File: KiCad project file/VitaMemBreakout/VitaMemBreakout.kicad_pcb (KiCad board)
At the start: 2 copper layers, 24.5 x 43 mm, 2 parts

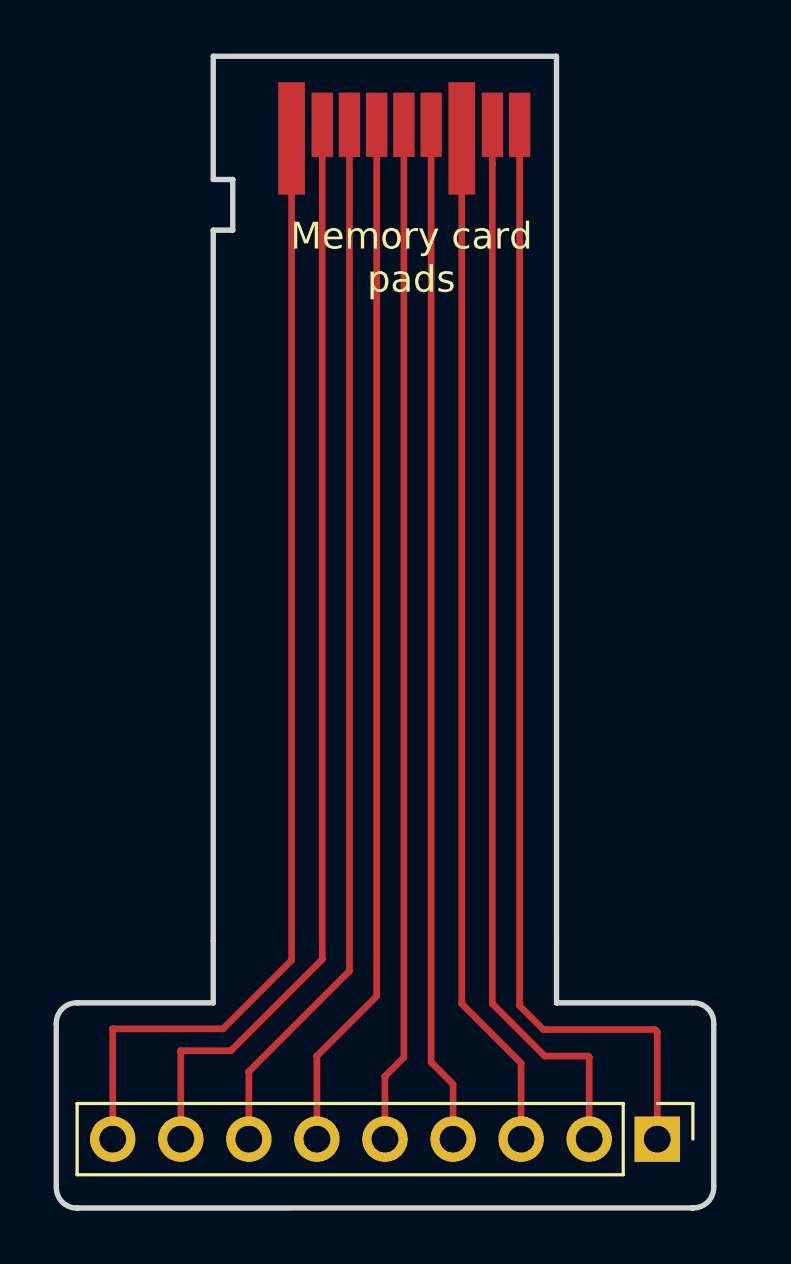
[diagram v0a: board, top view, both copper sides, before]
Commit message: Updated Pins
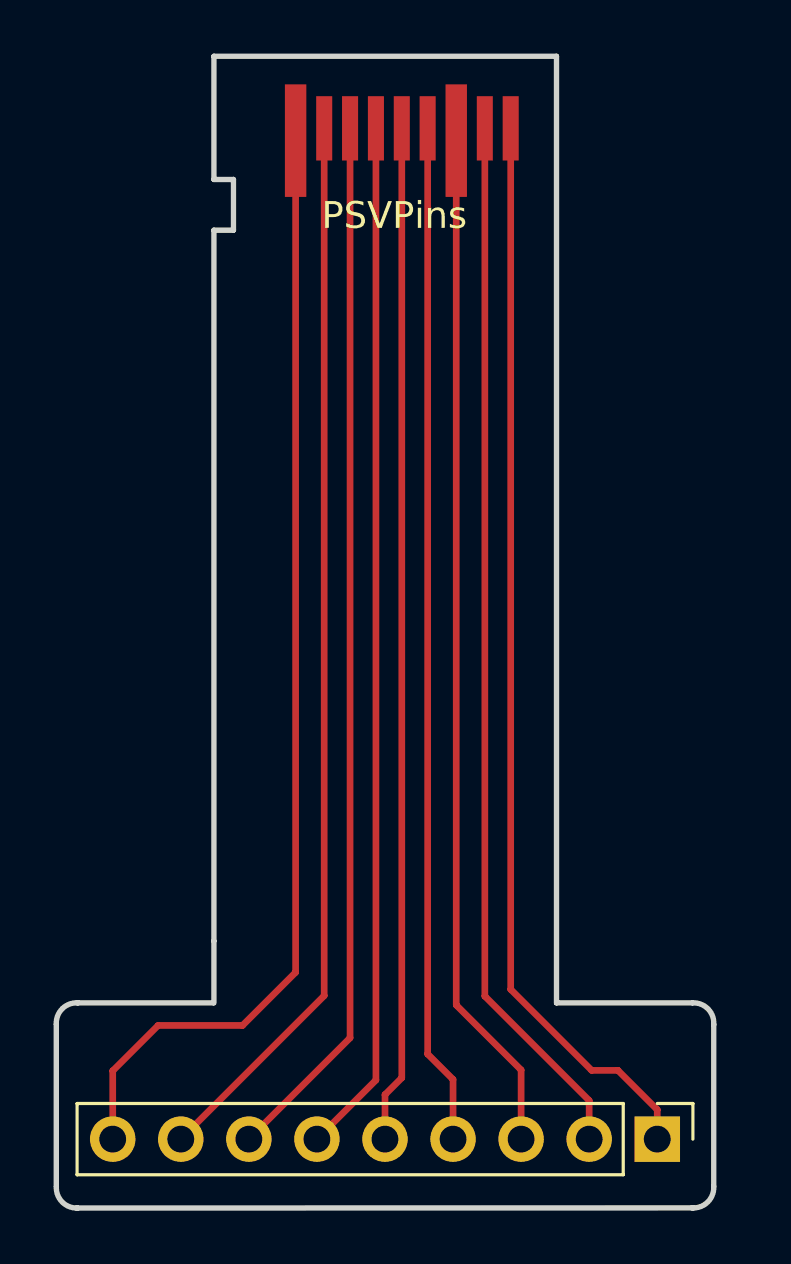
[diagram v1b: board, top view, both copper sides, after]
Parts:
- removed the ? at (30.3, 17.3)
- added PSVPins: , PSVita:PSVitaEdgeConnector, F.Cu at (30.5, 17.3)
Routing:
- net (no net): track 359.2 -> 354.0 mm
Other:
- board text removed: "Memory card pads"

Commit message: Hopefully perfect
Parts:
- removed PSVPins: , PSVita:PSVitaEdgeConnector
- added ?: , PSVita:PSVitaEdgeConnector, F.Cu at (30.4, 17.3)
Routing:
- net (no net): track 354.0 -> 352.3 mm
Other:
- outline, holes or cut-outs redrawn
- board text added: "By motoharu & TakuyaKou"

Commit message: V.Final
Production ready!
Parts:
- moved ? 0.40 mm to (39.3, 55.2)
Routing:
- net (no net): track 352.3 -> 353.2 mm
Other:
- board size 24.5 x 43 mm -> 25.3 x 43 mm
- board text added: "v 0.999"
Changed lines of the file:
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@@
   (general
     (thickness 1.6)
-    (drawings 21)
+    (drawings 22)
     (tracks 18)
     (zones 0)
@@
     (34 B.Paste user)
     (35 F.Paste user)
-    (36 B.SilkS user hide)
+    (36 B.SilkS user)
     (37 F.SilkS user)
     (38 B.Mask user)
@@
   )
   (module Connector_PinHeader_2.54mm:PinHeader_1x09_P2.54mm_Vertical (layer F.Cu)
-    (at 38.89502 55.118 270)
+    (at 39.2938 55.1688 270)
     (descr "Through hole straight pin header, 1x09, 2.54mm pitch, single row")
     (tags "Through hole pin header THT 1x09 2.54mm single row")
@@
     )
   )
-  (gr_text "By motoharu & TakuyaKou" (at 32.258 36.576 90) (layer B.SilkS)
+  (gr_text "v 0.999" (at 20.7645 51.6128) (layer B.SilkS)
+    (effects (font (size 1 1) (thickness 0.25)) (justify mirror))
+  )
+  (gr_text "By motoharu & TakuyaKou" (at 32.7025 31.5976 90) (layer B.SilkS)
     (effects (font (size 1.5 1.5) (thickness 0.3)) (justify mirror))
   )
   (gr_line (start 35.13582 47.72914) (end 35.13582 14.70914) (layer Edge.Cuts) (width 0.2))
   (gr_arc (start 17.228796 56.930987) (end 16.471876 56.885267) (angle -96.1) (layer Edge.Cuts) (width 0.2))
-  (gr_arc (start 40.245756 56.926504) (end 40.200036 57.683424) (angle -96.1) (layer Edge.Cuts) (width 0.2))
-  (gr_line (start 17.23898 57.68848) (end 40.23614 57.6834) (layer Edge.Cuts) (width 0.2))
-  (gr_line (start 35.13582 49.5554) (end 40.20566 49.5554) (layer Edge.Cuts) (width 0.2))
+  (gr_arc (start 41.025507 56.92648) (end 40.979787 57.6834) (angle -96.1) (layer Edge.Cuts) (width 0.2))
+  (gr_line (start 17.23898 57.68848) (end 40.9829 57.6834) (layer Edge.Cuts) (width 0.2))
+  (gr_line (start 35.13582 49.5554) (end 41.0083 49.5554) (layer Edge.Cuts) (width 0.2))
   (gr_line (start 35.13582 49.5554) (end 35.13582 47.75708) (layer Edge.Cuts) (width 0.2))
-  (gr_line (start 41.00576 50.3555) (end 41.00322 56.87568) (layer Edge.Cuts) (width 0.2))
+  (gr_line (start 41.783 50.3301) (end 41.783 56.896) (layer Edge.Cuts) (width 0.2))
   (gr_line (start 16.46936 50.31994) (end 16.46936 56.87568) (layer Edge.Cuts) (width 0.2))
   (gr_line (start 22.352 49.5554) (end 17.28216 49.5554) (layer Edge.Cuts) (width 0.2))
   (gr_line (start 22.352 47.73168) (end 22.352 49.5554) (layer Edge.Cuts) (width 0.2))
-  (gr_arc (start 40.251218 50.308892) (end 41.003058 50.369852) (angle -97.3) (layer Edge.Cuts) (width 0.2))
+  (gr_arc (start 41.03116 50.308892) (end 41.783 50.369852) (angle -97.3) (layer Edge.Cuts) (width 0.2))
   (gr_arc (start 17.22628 50.31232) (end 17.272 49.5554) (angle -96.1) (layer Edge.Cuts) (width 0.2))
   (gr_line (start 22.352 21.19884) (end 22.352 47.71644) (layer Margin) (width 0.2))
@@
   (gr_line (start 22.352 19.30654) (end 22.352 14.70914) (layer Edge.Cuts) (width 0.2))
   (gr_line (start 22.352 21.19884) (end 22.352 47.71644) (layer Edge.Cuts) (width 0.2))
-  (gr_text "PSVita Memory card\nbreakout adapter\n" (at 26.416 36.322 90) (layer B.SilkS)
+  (gr_text "PSVita Memory card\nbreakout adapter\n" (at 26.2636 32.1437 90) (layer B.SilkS)
     (effects (font (size 1.2 1.2) (thickness 0.3)) (justify mirror))
   )
   (gr_line (start 35.13582 14.70914) (end 22.352 14.70914) (layer Edge.Cuts) (width 0.2))
-  (segment (start 26.3906 49.84242) (end 26.3906 17.3482) (width 0.25) (layer F.Cu) (net 0))
-  (segment (start 21.11502 55.118) (end 26.3906 49.84242) (width 0.25) (layer F.Cu) (net 0))
-  (segment (start 27.305 51.46802) (end 23.65502 55.118) (width 0.25) (layer F.Cu) (net 0))
-  (segment (start 27.305 17.3482) (end 27.305 51.46802) (width 0.25) (layer F.Cu) (net 0))
-  (segment (start 28.2194 53.09362) (end 28.2194 17.3482) (width 0.25) (layer F.Cu) (net 0))
-  (segment (start 26.19502 55.118) (end 28.2194 53.09362) (width 0.25) (layer F.Cu) (net 0))
-  (segment (start 30.0482 53.89118) (end 31.27502 55.118) (width 0.25) (layer F.Cu) (net 0))
-  (segment (start 30.0482 17.3482) (end 30.0482 53.89118) (width 0.25) (layer F.Cu) (net 0))
-  (segment (start 31.0896 52.39258) (end 33.81502 55.118) (width 0.25) (layer F.Cu) (net 0))
-  (segment (start 31.0896 17.8054) (end 31.0896 52.39258) (width 0.25) (layer F.Cu) (net 0))
-  (segment (start 32.131 50.89398) (end 36.35502 55.118) (width 0.25) (layer F.Cu) (net 0))
-  (segment (start 32.131 17.3482) (end 32.131 50.89398) (width 0.25) (layer F.Cu) (net 0))
-  (segment (start 33.0454 49.26838) (end 38.89502 55.118) (width 0.25) (layer F.Cu) (net 0))
-  (segment (start 33.0454 17.3482) (end 33.0454 49.26838) (width 0.25) (layer F.Cu) (net 0))
-  (segment (start 25.3492 48.34382) (end 25.3492 17.8054) (width 0.25) (layer F.Cu) (net 0))
-  (segment (start 18.57502 55.118) (end 25.3492 48.34382) (width 0.25) (layer F.Cu) (net 0))
   (segment (start 29.1338 54.71922) (end 28.73502 55.118) (width 0.25) (layer F.Cu) (net 0))
-  (segment (start 29.1338 17.3482) (end 29.1338 54.71922) (width 0.25) (layer F.Cu) (net 0))
+  (segment (start 29.1338 17.3482) (end 29.1338 55.1688) (width 0.25) (layer F.Cu) (net 0))
+  (segment (start 25.3492 48.7934) (end 18.9738 55.1688) (width 0.25) (layer F.Cu) (net 0))
+  (segment (start 25.3492 17.8054) (end 25.3492 48.7934) (width 0.25) (layer F.Cu) (net 0))
+  (segment (start 26.3906 50.292) (end 21.5138 55.1688) (width 0.25) (layer F.Cu) (net 0))
+  (segment (start 26.3906 17.3482) (end 26.3906 50.292) (width 0.25) (layer F.Cu) (net 0))
+  (segment (start 27.305 51.9176) (end 24.0538 55.1688) (width 0.25) (layer F.Cu) (net 0))
+  (segment (start 27.305 17.3482) (end 27.305 51.9176) (width 0.25) (layer F.Cu) (net 0))
+  (segment (start 28.2194 53.5432) (end 26.5938 55.1688) (width 0.25) (layer F.Cu) (net 0))
+  (segment (start 28.2194 17.3482) (end 28.2194 53.5432) (width 0.25) (layer F.Cu) (net 0))
+  (segment (start 30.0482 53.5432) (end 31.6738 55.1688) (width 0.25) (layer F.Cu) (net 0))
+  (segment (start 30.0482 17.3482) (end 30.0482 53.5432) (width 0.25) (layer F.Cu) (net 0))
+  (segment (start 31.0896 52.0446) (end 34.2138 55.1688) (width 0.25) (layer F.Cu) (net 0))
+  (segment (start 31.0896 17.8054) (end 31.0896 52.0446) (width 0.25) (layer F.Cu) (net 0))
+  (segment (start 32.131 50.546) (end 36.7538 55.1688) (width 0.25) (layer F.Cu) (net 0))
+  (segment (start 32.131 17.3482) (end 32.131 50.546) (width 0.25) (layer F.Cu) (net 0))
+  (segment (start 33.0454 48.9204) (end 39.2938 55.1688) (width 0.25) (layer F.Cu) (net 0))
+  (segment (start 33.0454 17.3482) (end 33.0454 48.9204) (width 0.25) (layer F.Cu) (net 0))
 )
